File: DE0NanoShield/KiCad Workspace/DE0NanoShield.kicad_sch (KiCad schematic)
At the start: 41 parts

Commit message: Encoder and LCD connections
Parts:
- removed J?: RJ45_Bel_SI-60062-F, Connector_RJ:RJ45_Bel_SI-60062-F, symbol Connector:RJ45_Bel_SI-60062-F
- removed J?: Conn_01x08, symbol Connector_Generic:Conn_01x08
- removed J?: USB_B_Micro, symbol Connector:USB_B_Micro
- removed J?: Conn_01x06, symbol Connector_Generic:Conn_01x06
- removed J?: Micro_SD_Card, symbol Connector:Micro_SD_Card
- added R? (x7): 4.7k, symbol Device:R
- added RV?: R_Potentiometer, symbol Device:R_Potentiometer
- added SW?: RotaryEncoder_Switch, symbol Device:RotaryEncoder_Switch
- added SW?: SW_SPDT, symbol Switch:SW_SPDT
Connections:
- net +3V3: now also J?.11 (Pin_11), R?.2, R?.2, SW?.1 (A), SW?.S2
- net GND: now also J?.1 (Pin_1), J?.12 (Pin_12), J?.16 (Pin_16), J?.5 (Pin_5), R?.1, RV?.1, SW?.3 (C), SW?.C
- net RS: now reaches J?.17 (Pin_17)
- net RS: now also J?.4 (Pin_4)
- net E: now reaches J?.18 (Pin_18)
- net E: now also J?.6 (Pin_6)
- net DB4: now reaches J?.19 (Pin_19)
- net DB4: now also J?.11 (Pin_11)
- net DB5: now reaches J?.20 (Pin_20)
- net DB5: now also J?.12 (Pin_12)
- net DB6: now reaches J?.21 (Pin_21)
- net DB6: now also J?.13 (Pin_13)
- net DB7: now reaches J?.22 (Pin_22)
- net DB7: now also J?.14 (Pin_14)
- net A: now reaches J?.23 (Pin_23)
- net A: now also R?.1
- net B: now reaches J?.24 (Pin_24)
- net B: now also R?.1
- net BTN: now reaches J?.25 (Pin_25)
- net BTN: now also R?.1
- net SWT: now reaches J?.26 (Pin_26)
- net SWT: now also R?.1
- net +5V: now reaches J?.15 (Pin_15)
- net +5V: now also J?.2 (Pin_2), RV?.3
- net at J?.3 (Pin_3): now also RV?.2
- new net: R?.2, R?.2, SW?.S1
- new net: R?.1, R?.2, SW?.A
- new net: R?.1, R?.2, SW?.B
- new net: R?.2, SW?.2 (B)
- no-connect marks 0 -> 4
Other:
- moved on the sheet: 10k, D?, J?, R?, SW?, U?

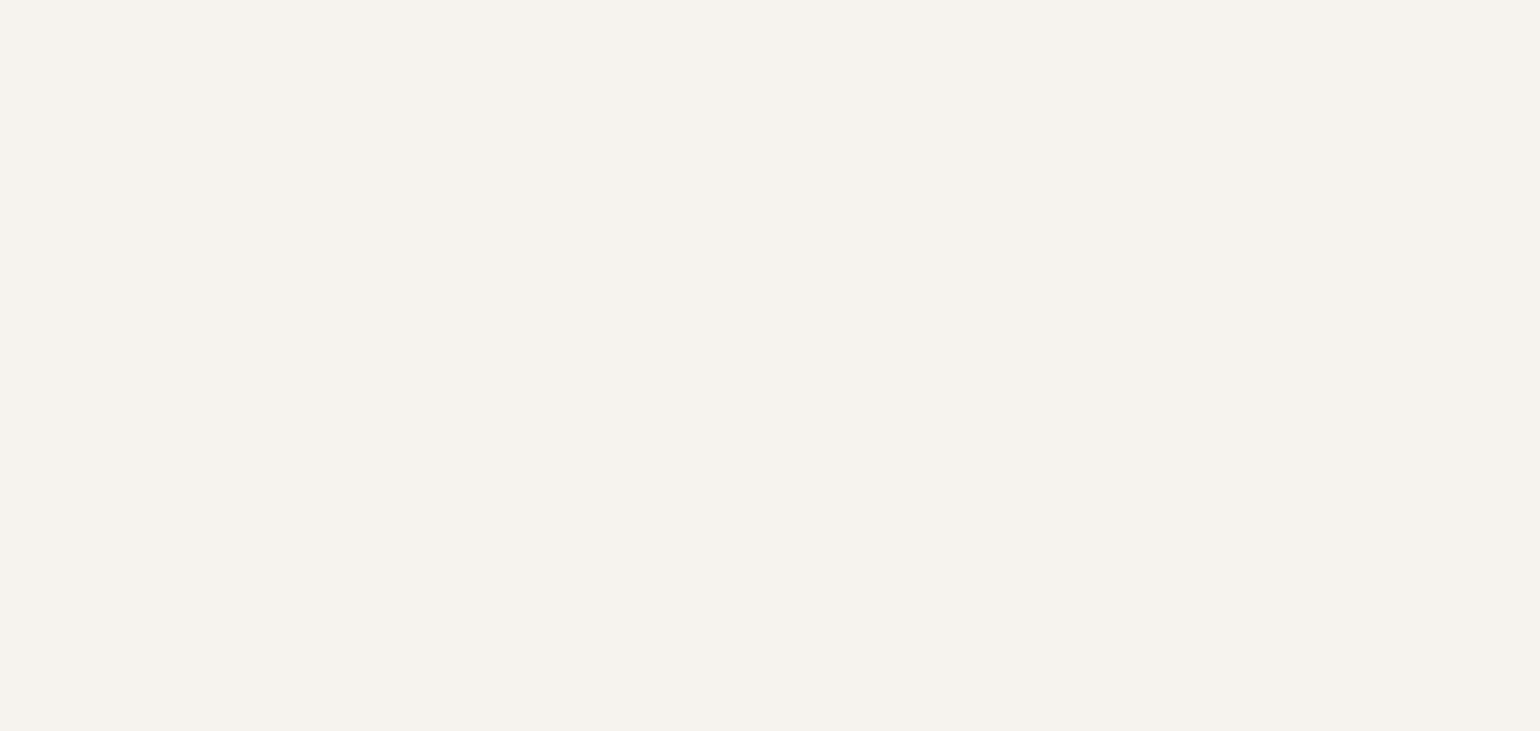
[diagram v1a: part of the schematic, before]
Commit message: Added audio circuit
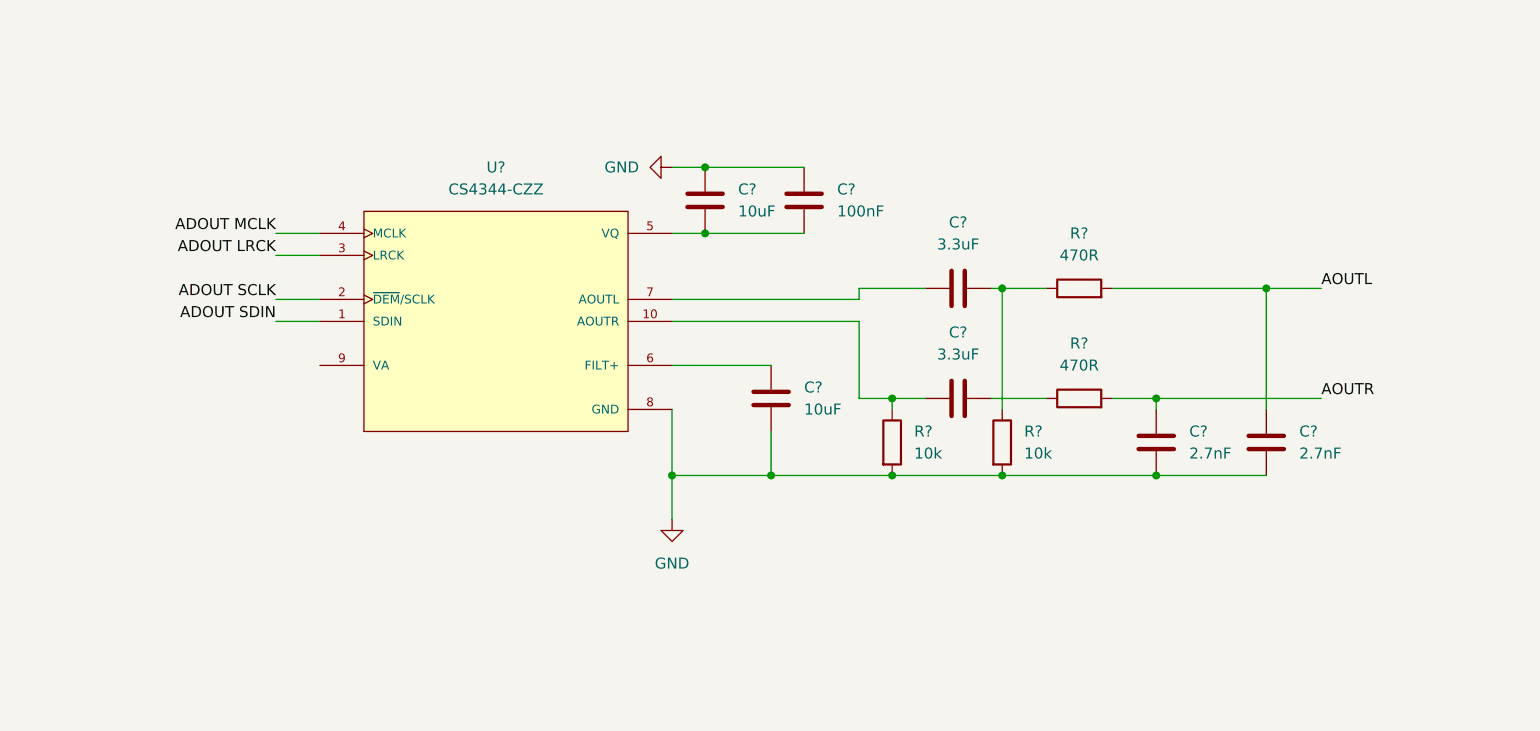
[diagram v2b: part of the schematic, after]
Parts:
- added C? (x2): 3.3uF, symbol Device:C
- added C? (x2): 10uF, symbol Device:C
- added C? (x2): 2.7nF, symbol Device:C
- added C?: 100nF, symbol Device:C
- added R? (x2): 10k, symbol Device:R
- added R? (x2): 470R, symbol Device:R
- added U?: CS4344-CZZ, SOP50P490X110-10N, symbol CS4344-CZZ:CS4344-CZZ
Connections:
- net GND: now also C?.1, C?.1, C?.2, C?.2, C?.2, R?.2, R?.2, U?.8 (GND)
- new net: C?.1, R?.1
- new net: C?.2, R?.1, U?.10 (AOUTR)
- new net: C?.1, U?.6 (FILT+)
- new net: C?.2, C?.2, U?.5 (VQ)
- new net: C?.2, U?.7 (AOUTL)
- new net: C?.1, R?.1, R?.1
- new net ADOUT LRCK: U?.3 (LRCK)
- new net ADOUT MCLK: U?.4 (MCLK)
- new net ADOUT SCLK: U?.2 (~{DEM}/SCLK)
- new net ADOUT SDIN: U?.1 (SDIN)
- new net AOUTL: C?.1, R?.2
- new net AOUTR: C?.1, R?.2

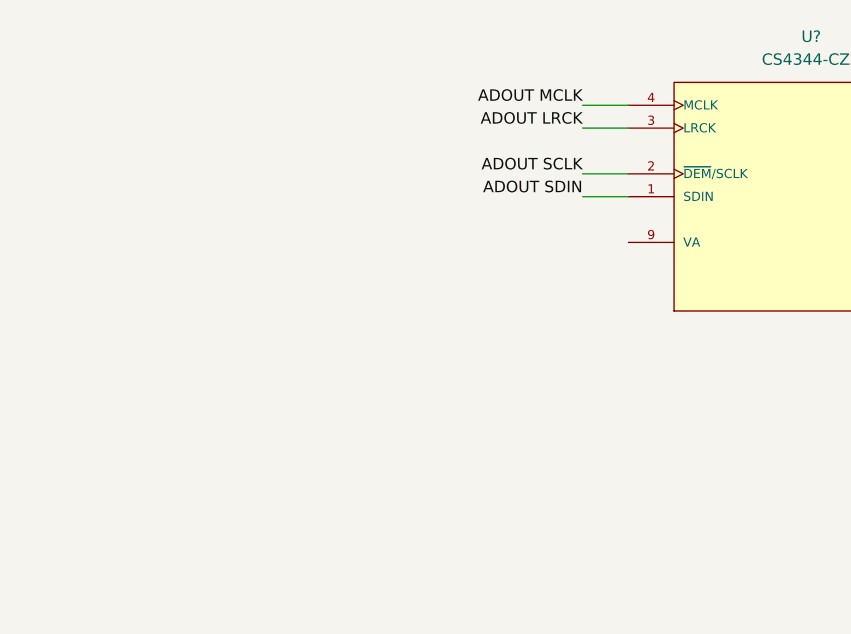
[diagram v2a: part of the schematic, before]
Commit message: Added audio DAC circuit
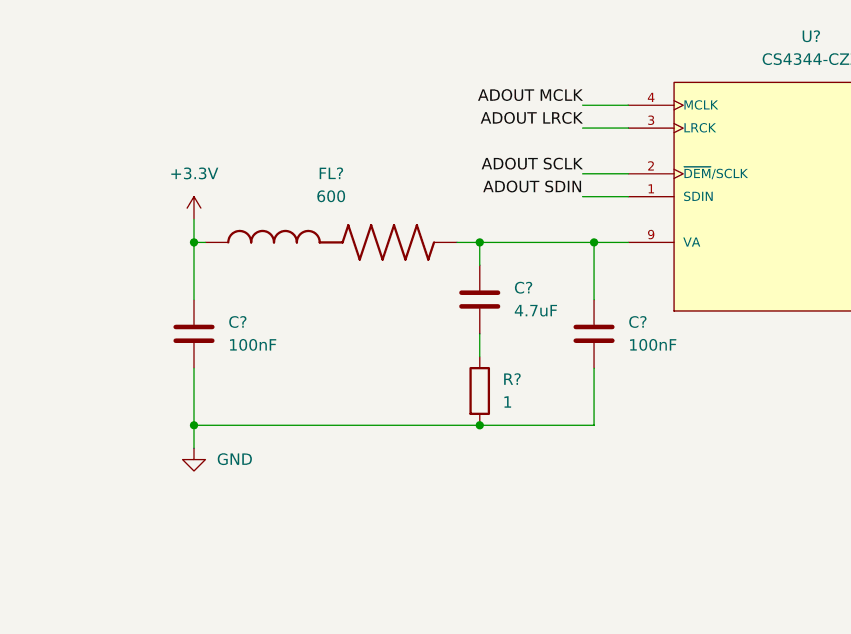
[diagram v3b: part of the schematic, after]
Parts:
- added C? (x2): 100nF, symbol Device:C
- added C?: 4.7uF, symbol Device:C
- added FL?: 600, BEADC1005X55N, symbol BLM15AG601SN1D:BLM15AG601SN1D
- added R?: 1, symbol Device:R
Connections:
- net +3V3: now also C?.1, FL?.1
- net GND: now also C?.2, C?.2, R?.2
- net at U?.9 (VA): now also C?.1, C?.1, FL?.2
- new net: C?.2, R?.1

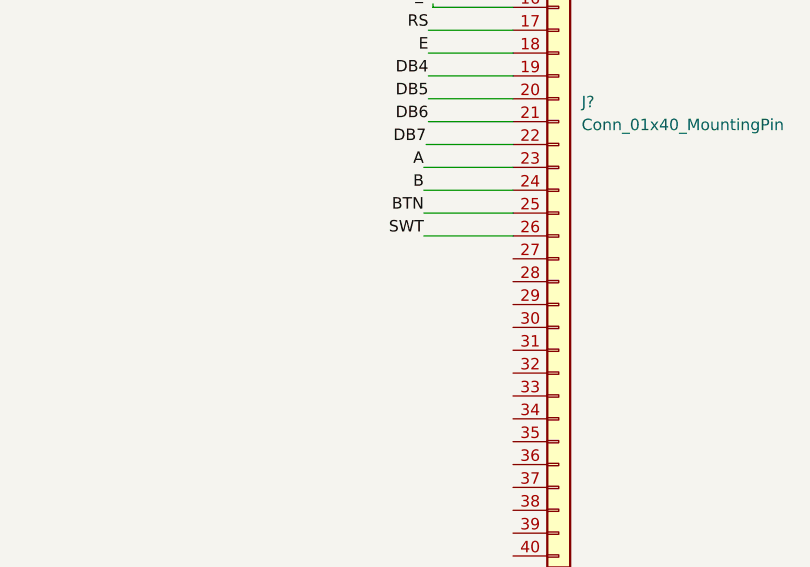
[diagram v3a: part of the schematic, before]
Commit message: Added labels for audio circuits
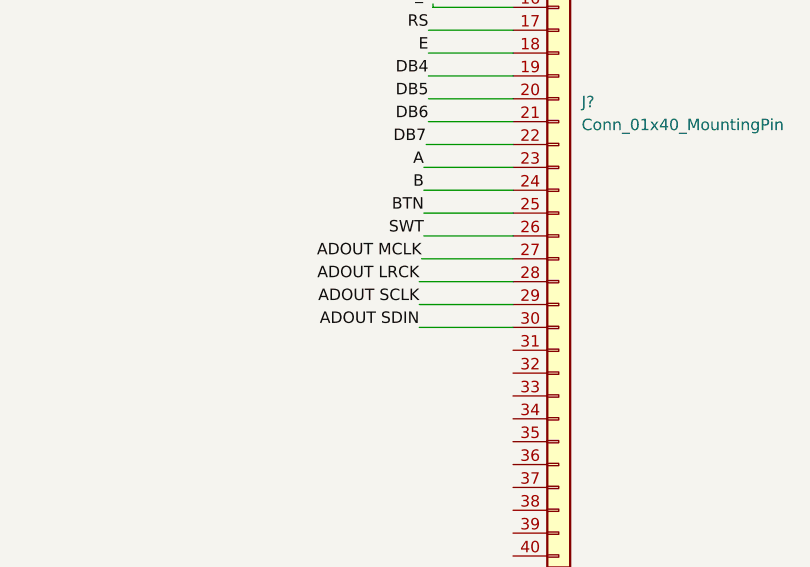
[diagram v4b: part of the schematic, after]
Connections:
- net ADOUT LRCK: now also J?.28 (Pin_28)
- net ADOUT MCLK: now also J?.27 (Pin_27)
- net ADOUT SCLK: now also J?.29 (Pin_29)
- net ADOUT SDIN: now also J?.30 (Pin_30)
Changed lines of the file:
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@@
+    (stroke (width 0) (type default) (color 0 0 0 0))
+  )
+  (wire (pts (xy 114.554 455.676) (xy 124.968 455.676))
     (stroke (width 0) (type default) (color 0 0 0 0))
   )
@@
     (stroke (width 0) (type default) (color 0 0 0 0))
   )
+  (wire (pts (xy 114.554 450.596) (xy 124.968 450.596))
+    (stroke (width 0) (type default) (color 0 0 0 0))
+  )
   (wire (pts (xy 110.49 300.99) (xy 78.74 300.99))
     (stroke (width 0) (type default) (color 0 0 0 0))
@@
     (stroke (width 0) (type default) (color 0 0 0 0))
   )
+  (wire (pts (xy 114.808 448.056) (xy 124.968 448.056))
+    (stroke (width 0) (type default) (color 0 0 0 0))
+  )
   (wire (pts (xy 45.847 102.87) (xy 48.26 102.87))
     (stroke (width 0) (type default) (color 0 0 0 0))
@@
     (stroke (width 0) (type default) (color 0 0 0 0))
   )
+  (wire (pts (xy 114.554 453.136) (xy 124.968 453.136))
+    (stroke (width 0) (type default) (color 0 0 0 0))
+  )
   (wire (pts (xy 362.839 65.405) (xy 362.839 79.883))
     (stroke (width 0) (type default) (color 0 0 0 0))
@@
     (effects (font (size 1.27 1.27)) (justify right bottom))
   )
+  (label "ADOUT SDIN" (at 114.554 455.676 180)
+    (effects (font (size 1.27 1.27)) (justify right bottom))
+  )
   (label "R_LED_1" (at 116.078 382.016 180)
     (effects (font (size 1.27 1.27)) (justify right bottom))
@@
     (effects (font (size 1.27 1.27)) (justify right bottom))
   )
+  (label "ADOUT LRCK" (at 114.554 450.596 180)
+    (effects (font (size 1.27 1.27)) (justify right bottom))
+  )
+  (label "ADOUT SCLK" (at 114.554 453.136 180)
+    (effects (font (size 1.27 1.27)) (justify right bottom))
+  )
   (label "SPDT_1" (at 115.951 407.289 180)
     (effects (font (size 1.27 1.27)) (justify right bottom))
@@
     (effects (font (size 1.27 1.27)) (justify right bottom))
   )
+  (label "ADOUT MCLK" (at 114.808 448.056 180)
+    (effects (font (size 1.27 1.27)) (justify right bottom))
+  )

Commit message: connector net labels added
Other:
- moved on the sheet: 10k, C?, D?, FL?, J?, R?, RV?, SW?, U?
